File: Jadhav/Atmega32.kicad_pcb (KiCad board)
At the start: 2 copper layers, 23 parts, among them SW1 SW_Push, U1 ATmega16A-AU, U2 NCP1117ST33T3G, Y1 8MHz, j1 62910416121

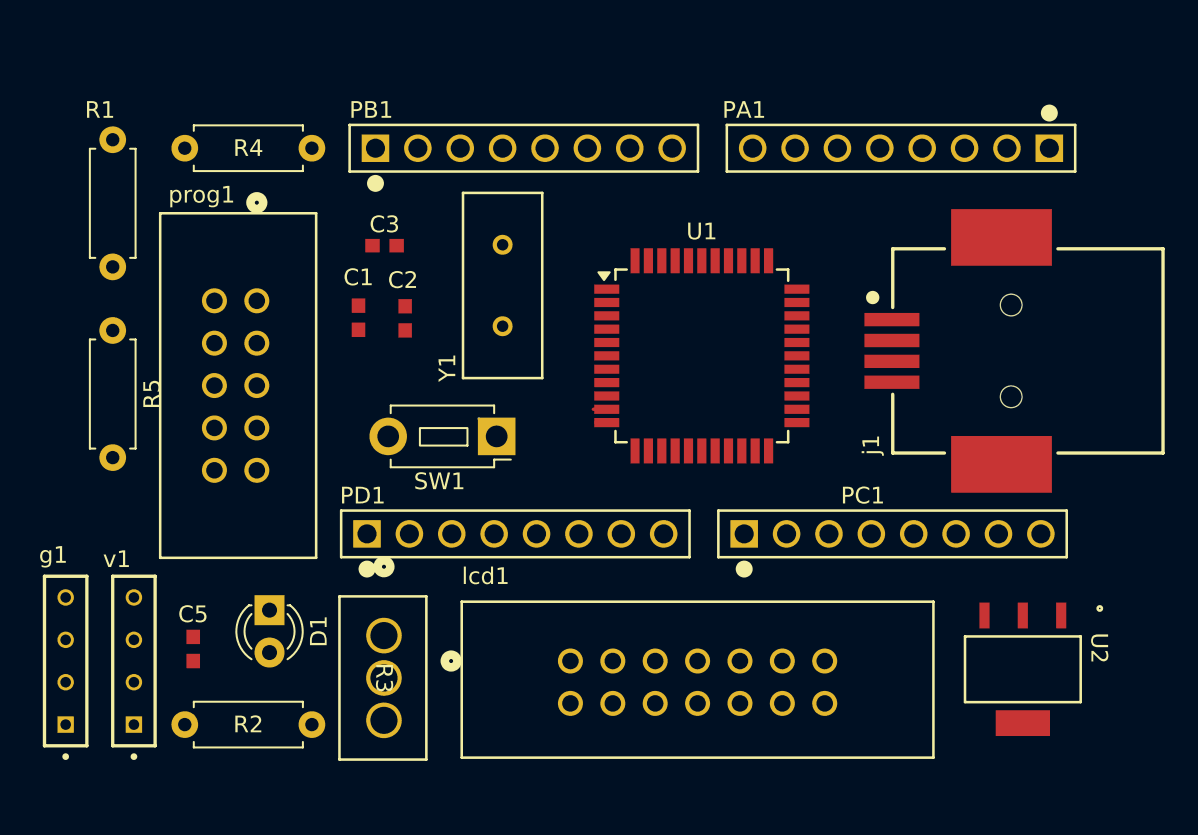
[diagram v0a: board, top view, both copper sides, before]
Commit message: Updated footprint for LCD
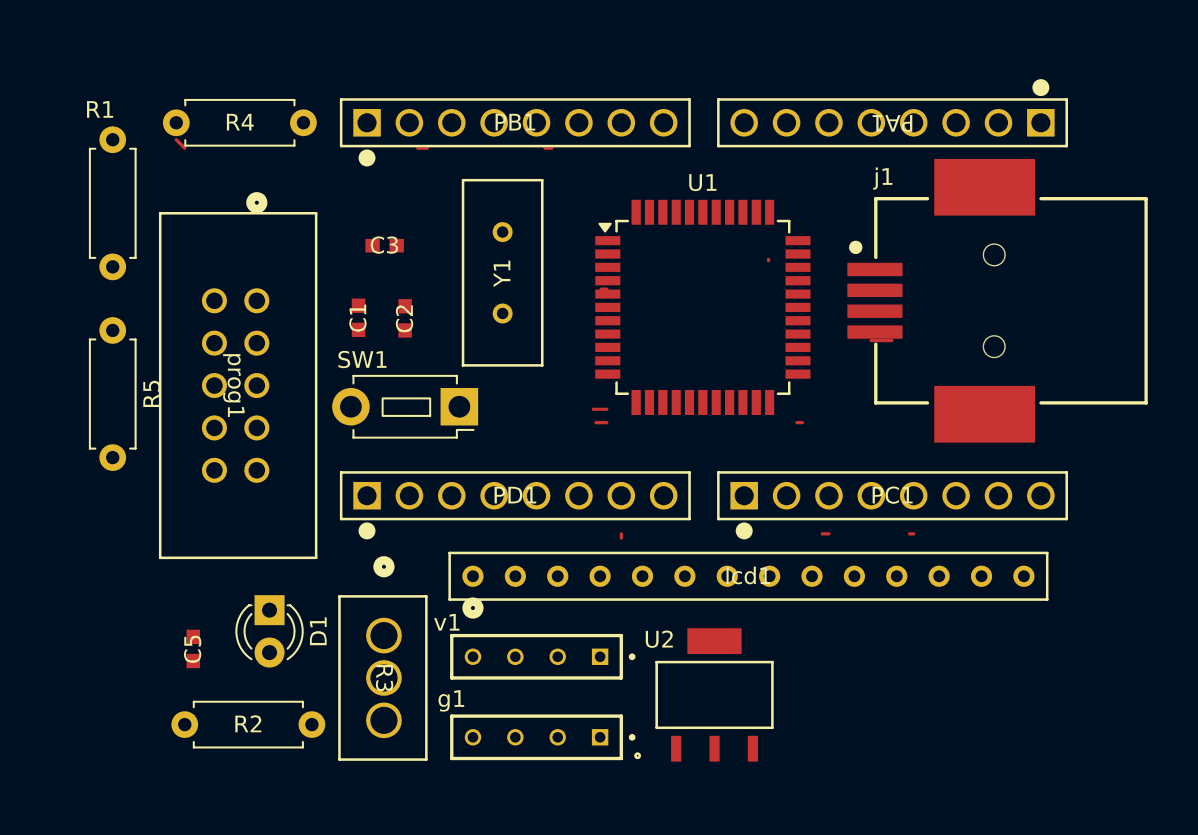
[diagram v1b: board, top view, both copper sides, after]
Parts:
- C1, C2, C3, C5: footprint J_footprint:G-188_MUR -> J_footprints:G-188_MUR
- PA1, PB1, PC1, PD1: footprint J_footprint:CONN8_61300811121_WRE -> J_footprints:CONN8_61300811121_WRE
- R3: footprint J_footprint:RES3_PV36W103C01B00_BRN -> J_footprints:RES3_PV36W103C01B00_BRN
- U2: footprint J_footprint:SOT223-3_ONS -> J_footprints:SOT223-3_ONS
- Y1: footprint J_footprint:ATS08A-E_CTS -> J_footprints:ATS08A-E_CTS
- g1, v1: footprint J_footprint:SAMTEC_TS-104-T-AA -> J_footprints:SAMTEC_TS-104-T-AA
- j1: footprint J_footprint:62910416121 -> J_footprints:62910416121
- lcd1: footprint J_footprint:14_CONN_SBH11-PBPC-D07-ST-BK_SUL -> J_footprints:CON14_1X14_TU_HTS_SAI
- prog1: footprint J_footprint:CONN_SBH11-PBPC-D05-ST-BK_SUL -> J_footprints:CONN_SBH11-PBPC-D05-ST-BK_SUL
- moved g1 28.6 mm to (160.8, 78.2), turned to 180 degrees
- moved v1 24.1 mm to (160.8, 73.4), turned to 180 degrees
- moved U2 18.5 mm to (171.4, 75.7), turned to 0 degrees
- moved lcd1 11.8 mm to (173.5, 68.6)
- moved j1 3.17 mm to (188.2, 52.1)
- moved U1 2.91 mm to (170.8, 52.5)
- moved SW1 2.86 mm to (156.2, 58.4)
- moved PC1 2.29 mm to (173.2, 63.8)
- moved PD1 2.29 mm to (150.6, 63.8)
- moved PA1 1.61 mm to (191.0, 41.4)
- moved PB1 1.61 mm to (150.6, 41.4)
- moved R4 1.61 mm to (139.2, 41.4)
- moved Y1 0.76 mm to (158.8, 52.8)
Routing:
- net GND: track 2.74 -> 0.00 mm
- net unconnected-(j1-D--Pad2): track 0.00 -> 1.25 mm

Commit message: Initial routing
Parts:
- moved v1 5.09 mm to (161.0, 78.5), turned to 0 degrees
- moved g1 4.07 mm to (161.0, 74.2), turned to 0 degrees
- moved D1 1.05 mm to (143.8, 70.9)
- moved C5 0.77 mm to (139.7, 72.4), turned to 0 degrees
- moved R3 0.57 mm to (151.1, 72.4)
- moved R2 0.57 mm to (146.8, 77.7)
- moved R5 0.51 mm to (135.4, 54.4)
- moved PD1 0.36 mm to (150.9, 63.5)
- moved PC1 0.25 mm to (173.2, 63.5)
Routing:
- net +5: track 1.77 -> 133.3 mm
- net /RESET: track 0.00 -> 82.3 mm, vias 0 -> 1
- net /MOSI: track 0.00 -> 71.7 mm, vias 0 -> 1
- net /SCK: track 0.00 -> 66.4 mm
- net Net-(U2-IN): track 0.00 -> 47.8 mm
- net Net-(U1-XTAL1): track 0.00 -> 46.4 mm
- net /MISO: track 0.56 -> 42.0 mm
- net /D7: track 0.00 -> 28.6 mm
- net Net-(U1-PB4_(~{SS})): track 0.00 -> 24.6 mm
- net Net-(U1-PA7_(ADC7)): track 0.00 -> 23.0 mm
- net /D6: track 0.00 -> 21.1 mm
- net /EN: track 0.00 -> 20.7 mm
- net Net-(U1-PA6_(ADC6)): track 0.00 -> 20.3 mm
- net /D5: track 0.00 -> 18.2 mm
- net Net-(U1-PD0_(RXD)): track 0.00 -> 17.8 mm
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
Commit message: Routing, Zone filling , todo : fix v1g1 errors
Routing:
- net GND: track 5.03 -> 111.3 mm, vias 0 -> 4
- net Net-(U1-AREF): track 0.00 -> 25.3 mm, vias 0 -> 2
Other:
- board outline added: 66.8 x 46 mm

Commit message: Grounding done , todo v1g1
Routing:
- net GND: track 111.3 -> 134.0 mm, vias 4 -> 6
- net Net-(U1-AREF): track 25.3 -> 27.4 mm
- net +5: track 132.9 -> 134.9 mm
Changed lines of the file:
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@@
-	)
-	(segment
-		(start 139.7 71.628)
-		(end 139.7 54.864)
-		(width 0.2)
-		(layer "F.Cu")
-		(net 2)
 	)
 	(segment
@@
 	)
 	(segment
+		(start 138.9761 72.3519)
+		(end 138.9761 57.9501)
+		(width 0.2)
+		(layer "F.Cu")
+		(net 2)
+	)
+	(segment
 		(start 154.686 69.342)
 		(end 154.686 76.2)
@@
 	)
 	(segment
-		(start 139.7 54.864)
-		(end 139.192 54.356)
+		(start 138.9761 57.9501)
+		(end 135.382 54.356)
 		(width 0.2)
 		(layer "F.Cu")
@@
 	)
 	(segment
+		(start 140.4239 72.3519)
+		(end 142.2781 72.3519)
+		(width 0.2)
+		(layer "F.Cu")
+		(net 6)
+	)
+	(segment
+		(start 175.55053 52.466)
+		(end 176.452 52.466)
+		(width 0.2)
+		(layer "F.Cu")
+		(net 6)
+	)
+	(segment
+		(start 142.2781 72.3519)
+		(end 143.764 70.866)
+		(width 0.2)
+		(layer "F.Cu")
+		(net 6)
+	)
+	(segment
 		(start 148.8107 63.2793)
 		(end 153.67 58.42)
@@
 	)
 	(segment
+		(start 170.752 49.212)
+		(end 170.18 49.784)
+		(width 0.2)
+		(layer "F.Cu")
+		(net 6)
+	)
+	(segment
 		(start 176.452 52.466)
 		(end 178.793 52.466)
@@
 	)
 	(segment
+		(start 174.826265 51.741735)
+		(end 175.55053 52.466)
+		(width 0.2)
+		(layer "F.Cu")
+		(net 6)
+	)
+	(segment
 		(start 153.416 58.42)
 		(end 156.158 58.42)
@@
 		(start 156.972 68.58)
 		(end 157.870025 68.58)
+		(width 0.2)
+		(layer "F.Cu")
+		(net 6)
+	)
+	(segment
+		(start 170.752 46.766)
+		(end 170.752 49.212)
 		(width 0.2)
 		(layer "F.Cu")
@@
 		(net 6)
 	)
+	(via
+		(at 174.826265 51.741735)
+		(size 0.6)
+		(drill 0.3)
+		(layers "F.Cu" "B.Cu")
+		(net 6)
+	)
+	(via
+		(at 170.18 49.784)
+		(size 0.6)
+		(drill 0.3)
+		(layers "F.Cu" "B.Cu")
+		(net 6)
+	)
 	(segment
 		(start 143.764 64.516)
@@
 	)
 	(segment
+		(start 171.45 53.086)
+		(end 172.974 51.562)
+		(width 0.2)
+		(layer "B.Cu")
+		(net 6)
+	)
+	(segment
+		(start 170.18 49.784)
+		(end 171.034 48.93)
+		(width 0.2)
+		(layer "B.Cu")
+		(net 6)
+	)
+	(segment
 		(start 161.544 54.666)
 		(end 161.544 53.34)
@@
 	)
 	(segment
+		(start 174.64653 51.562)
+		(end 174.826265 51.741735)
+		(width 0.2)
+		(layer "B.Cu")
+		(net 6)
+	)
+	(segment
 		(start 169.531 53.481)
 		(end 171.45 55.4)
@@
 	)
 	(segment
+		(start 171.034 48.93)
+		(end 173.730529 48.93)
+		(width 0.2)
+		(layer "B.Cu")
+		(net 6)
+	)
+	(segment
+		(start 173.730529 48.93)
+		(end 174.826265 50.025736)
+		(width 0.2)
+		(layer "B.Cu")
+		(net 6)
+	)
+	(segment
+		(start 172.974 51.562)
+		(end 174.64653 51.562)
+		(width 0.2)
+		(layer "B.Cu")
+		(net 6)
+	)
+	(segment
+		(start 174.826265 50.025736)
+		(end 174.826265 51.741735)
+		(width 0.2)
+		(layer "B.Cu")
+		(net 6)
+	)
+	(segment
 		(start 171.45 55.4)
 		(end 171.45 55.88)
@@
 		(start 141.478 62.23)
 		(end 143.764 64.516)
+		(width 0.2)
+		(layer "B.Cu")
+		(net 6)
+	)
+	(segment
+		(start 171.45 55.4)
+		(end 171.45 53.086)
 		(width 0.2)
 		(layer "B.Cu")
@@
 	)
 	(segment
-		(start 174.752 51.562)
-		(end 176.348 51.562)
+		(start 173.482 49.53)
+		(end 174.244 49.53)
+		(width 0.2)
+		(layer "F.Cu")
+		(net 31)
+	)
+	(segment
+		(start 175.402 50.688)
+		(end 175.402 51.441)
+		(width 0.2)
+		(layer "F.Cu")
+		(net 31)
+	)
+	(segment
+		(start 174.244 49.53)
+		(end 175.402 50.688)
 		(width 0.2)
 		(layer "F.Cu")
@@
 	)
 	(segment
-		(start 176.348 51.562)
+		(start 175.627 51.666)
 		(end 176.452 51.666)
 		(width 0.2)
@@
 		(net 31)
 	)
+	(segment
+		(start 175.402 51.441)
+		(end 175.627 51.666)
+		(width 0.2)
+		(layer "F.Cu")
+		(net 31)
+	)
 	(via
-		(at 174.752 51.562)
+		(at 173.482 49.53)
 		(size 0.6)
 		(drill 0.3)
@@
 	)
 	(segment
-		(start 155.448 51.562)
-		(end 174.752 51.562)
-		(width 0.2)
-		(layer "B.Cu")
+		(start 173.482 49.53)
+		(end 171.45 51.562)
+		(width 0.2)
+		(layer "B.Cu")
+		(net 31)
+	)
+	(segment
+		(start 171.45 51.562)
+		(end 155.448 51.562)
+		(width 0.2)
+		(layer "B.Cu")

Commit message: g1 v1 fixed
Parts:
- g1, v1: footprint J_footprints:SAMTEC_TS-104-T-AA -> J_footprints:CON4_1X4_TU_HTS_SAI
- moved g1 0.57 mm to (160.8, 73.7)
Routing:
- net +5: track 134.9 -> 146.2 mm
- net GND: track 134.0 -> 136.7 mm
